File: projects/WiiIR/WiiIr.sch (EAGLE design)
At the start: 20 parts

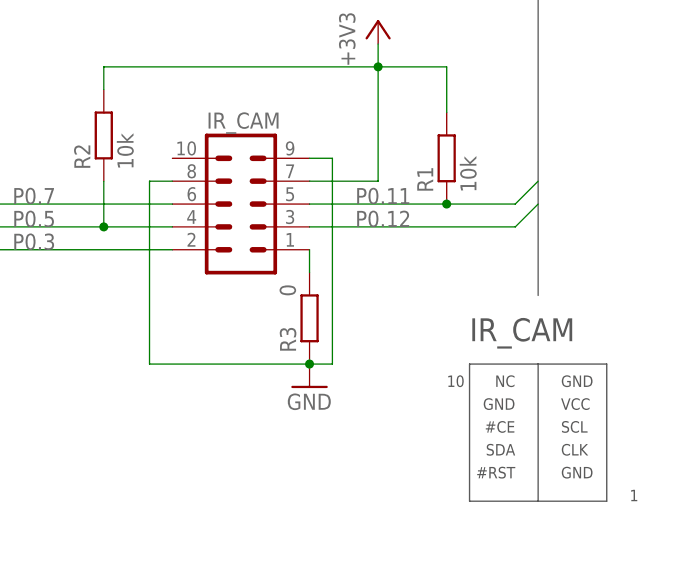
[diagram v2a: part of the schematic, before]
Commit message: Updated CamAdapter + Board
* Added 25 MHz resonator to adapter board
* Removed 25 MHz CLK signal from PCB connector
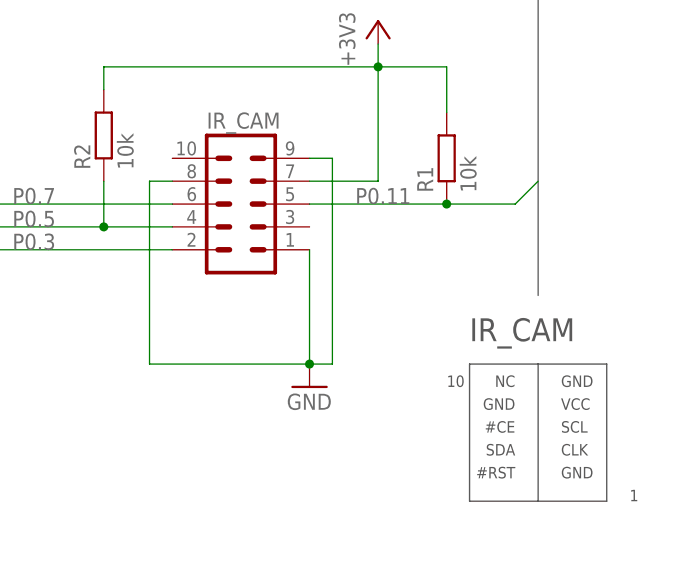
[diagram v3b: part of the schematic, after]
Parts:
- removed R3: 0, resistor:R-EU_0207/10
- R1: device resistor:R-EU_0207/15 -> resistor:R-EU_0207/12
- SV1, SV2: device con-lstb:MA20-2BIG -> con-lstb:MA20-2
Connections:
- removed net N$12: IR_CAM.1, R3.1
- net GND: now also IR_CAM.1; no longer R3.2
- net P0.12: no longer IR_CAM.3
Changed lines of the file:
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@@
 <grid distance="0.1" unitdist="inch" unit="inch" style="lines" multiple="1" display="no" altdistance="0.01" altunitdist="inch" altunit="inch"/>
 <layers>
-<layer number="1" name="Top" color="4" fill="1" visible="no" active="no"/>
-<layer number="16" name="Bottom" color="1" fill="1" visible="no" active="no"/>
-<layer number="17" name="Pads" color="2" fill="1" visible="no" active="no"/>
-<layer number="18" name="Vias" color="2" fill="1" visible="no" active="no"/>
-<layer number="19" name="Unrouted" color="6" fill="1" visible="no" active="no"/>
-<layer number="20" name="Dimension" color="15" fill="1" visible="no" active="no"/>
-<layer number="21" name="tPlace" color="7" fill="1" visible="no" active="no"/>
-<layer number="22" name="bPlace" color="7" fill="1" visible="no" active="no"/>
-<layer number="23" name="tOrigins" color="15" fill="1" visible="no" active="no"/>
-<layer number="24" name="bOrigins" color="15" fill="1" visible="no" active="no"/>
-<layer number="25" name="tNames" color="7" fill="1" visible="no" active="no"/>
-<layer number="26" name="bNames" color="7" fill="1" visible="no" active="no"/>
-<layer number="27" name="tValues" color="7" fill="1" visible="no" active="no"/>
-<layer number="28" name="bValues" color="7" fill="1" visible="no" active="no"/>
+<layer number="1" name="Top" color="4" fill="1" visible="yes" active="no"/>
+<layer number="16" name="Bottom" color="1" fill="1" visible="yes" active="no"/>
+<layer number="17" name="Pads" color="2" fill="1" visible="yes" active="no"/>
+<layer number="18" name="Vias" color="2" fill="1" visible="yes" active="no"/>
+<layer number="19" name="Unrouted" color="6" fill="1" visible="yes" active="no"/>
+<layer number="20" name="Dimension" color="15" fill="1" visible="yes" active="no"/>
+<layer number="21" name="tPlace" color="7" fill="1" visible="yes" active="no"/>
+<layer number="22" name="bPlace" color="7" fill="1" visible="yes" active="no"/>
+<layer number="23" name="tOrigins" color="15" fill="1" visible="yes" active="no"/>
+<layer number="24" name="bOrigins" color="15" fill="1" visible="yes" active="no"/>
+<layer number="25" name="tNames" color="7" fill="1" visible="yes" active="no"/>
+<layer number="26" name="bNames" color="7" fill="1" visible="yes" active="no"/>
+<layer number="27" name="tValues" color="7" fill="1" visible="yes" active="no"/>
+<layer number="28" name="bValues" color="7" fill="1" visible="yes" active="no"/>
 <layer number="29" name="tStop" color="7" fill="3" visible="no" active="no"/>
 <layer number="30" name="bStop" color="7" fill="6" visible="no" active="no"/>
@@
 <layer number="35" name="tGlue" color="7" fill="4" visible="no" active="no"/>
 <layer number="36" name="bGlue" color="7" fill="5" visible="no" active="no"/>
-<layer number="37" name="tTest" color="7" fill="1" visible="no" active="no"/>
-<layer number="38" name="bTest" color="7" fill="1" visible="no" active="no"/>
+<layer number="37" name="tTest" color="7" fill="1" visible="yes" active="no"/>
+<layer number="38" name="bTest" color="7" fill="1" visible="yes" active="no"/>
 <layer number="39" name="tKeepout" color="4" fill="11" visible="no" active="no"/>
 <layer number="40" name="bKeepout" color="1" fill="11" visible="no" active="no"/>
@@
 <layer number="44" name="Drills" color="7" fill="1" visible="no" active="no"/>
 <layer number="45" name="Holes" color="7" fill="1" visible="no" active="no"/>
-<layer number="46" name="Milling" color="3" fill="1" visible="no" active="no"/>
-<layer number="47" name="Measures" color="7" fill="1" visible="no" active="no"/>
-<layer number="48" name="Document" color="7" fill="1" visible="no" active="no"/>
-<layer number="49" name="Reference" color="7" fill="1" visible="no" active="no"/>
-<layer number="51" name="tDocu" color="7" fill="1" visible="no" active="no"/>
-<layer number="52" name="bDocu" color="7" fill="1" visible="no" active="no"/>
+<layer number="46" name="Milling" color="3" fill="1" visible="yes" active="no"/>
+<layer number="47" name="Measures" color="7" fill="1" visible="yes" active="no"/>
+<layer number="48" name="Document" color="7" fill="1" visible="yes" active="no"/>
+<layer number="49" name="Reference" color="7" fill="1" visible="yes" active="no"/>
+<layer number="51" name="tDocu" color="7" fill="1" visible="yes" active="no"/>
+<layer number="52" name="bDocu" color="7" fill="1" visible="yes" active="no"/>
 <layer number="91" name="Nets" color="2" fill="1" visible="yes" active="yes"/>
 <layer number="92" name="Busses" color="1" fill="1" visible="yes" active="yes"/>
@@
 </classes>
 <parts>
-<part name="SV1" library="con-lstb" deviceset="MA20-2" device="BIG"/>
-<part name="SV2" library="con-lstb" deviceset="MA20-2" device="BIG"/>
+<part name="SV1" library="con-lstb" deviceset="MA20-2" device=""/>
+<part name="SV2" library="con-lstb" deviceset="MA20-2" device=""/>
 <part name="GND1" library="supply1" deviceset="GND" device=""/>
 <part name="GND2" library="supply1" deviceset="GND" device=""/>
@@
 <part name="GND8" library="supply1" deviceset="GND" device=""/>
 <part name="+3V6" library="supply1" deviceset="+3V3" device=""/>
-<part name="R1" library="resistor" deviceset="R-EU_" device="0207/15" value="10k"/>
+<part name="R1" library="resistor" deviceset="R-EU_" device="0207/12" value="10k"/>
 <part name="R2" library="resistor" deviceset="R-EU_" device="0207/10" value="10k"/>
 <part name="DBG_R" library="resistor-sil" deviceset="G08R" device="" value="100"/>
@@
 <part name="MOTOR" library="pinhead" deviceset="PINHD-1X3" device="/90"/>
 <part name="SERVO" library="pinhead" deviceset="PINHD-1X3" device="/90"/>
-<part name="R3" library="resistor" deviceset="R-EU_" device="0207/10" value="0"/>
 </parts>
 <sheets>
@@
 <instance part="MOTOR" gate="A" x="210.82" y="142.24"/>
 <instance part="SERVO" gate="A" x="210.82" y="116.84"/>
-<instance part="R3" gate="G$1" x="213.36" y="66.04" smashed="yes" rot="R270">
-<attribute name="NAME" x="211.8614" y="62.23" size="1.778" layer="95" rot="R90"/>
-<attribute name="VALUE" x="210.058" y="69.85" size="1.778" layer="96" rot="R270"/>
-</instance>
 </instances>
 <busses>
@@
 <wire x1="195.58" y1="81.28" x2="195.58" y2="60.96" width="0.1524" layer="91"/>
 <wire x1="195.58" y1="60.96" x2="213.36" y2="60.96" width="0.1524" layer="91"/>
-<pinref part="R3" gate="G$1" pin="2"/>
 <junction x="213.36" y="60.96"/>
 <pinref part="IR_CAM" gate="G$1" pin="9"/>
@@
 <wire x1="215.9" y1="83.82" x2="215.9" y2="60.96" width="0.1524" layer="91"/>
 <wire x1="215.9" y1="60.96" x2="213.36" y2="60.96" width="0.1524" layer="91"/>
+<pinref part="IR_CAM" gate="G$1" pin="1"/>
+<wire x1="213.36" y1="73.66" x2="213.36" y2="60.96" width="0.1524" layer="91"/>
 </segment>
 <segment>
@@
 <label x="170.18" y="134.62" size="1.778" layer="95" rot="MR0"/>
 </segment>
-<segment>
-<pinref part="IR_CAM" gate="G$1" pin="3"/>
-<wire x1="213.36" y1="76.2" x2="236.22" y2="76.2" width="0.1524" layer="91"/>
-<wire x1="236.22" y1="76.2" x2="238.76" y2="78.74" width="0.1524" layer="91"/>
-<label x="218.44" y="76.2" size="1.778" layer="95"/>
-</segment>
 </net>
 <net name="P0.6" class="0">
@@
 </segment>
 </net>
-<net name="N$12" class="0">
-<segment>
-<pinref part="R3" gate="G$1" pin="1"/>
-<pinref part="IR_CAM" gate="G$1" pin="1"/>
-<wire x1="213.36" y1="73.66" x2="213.36" y2="71.12" width="0.1524" layer="91"/>
-</segment>
-</net>
